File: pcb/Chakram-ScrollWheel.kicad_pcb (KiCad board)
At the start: 2 copper layers, 39.7 x 22.2 mm, 16 parts, among them J1 FPC Connector, SW1 RotaryEncoder

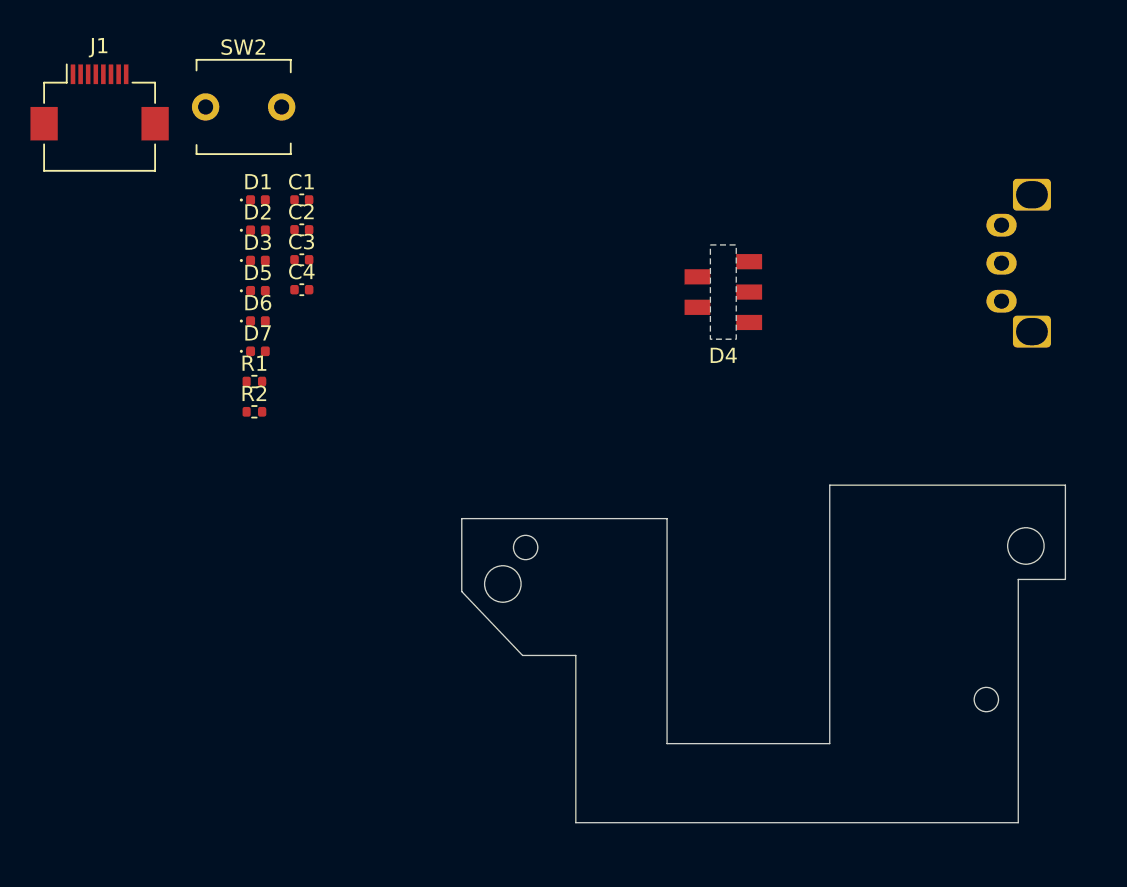
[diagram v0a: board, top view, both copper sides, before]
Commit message: Updated hole and component positions
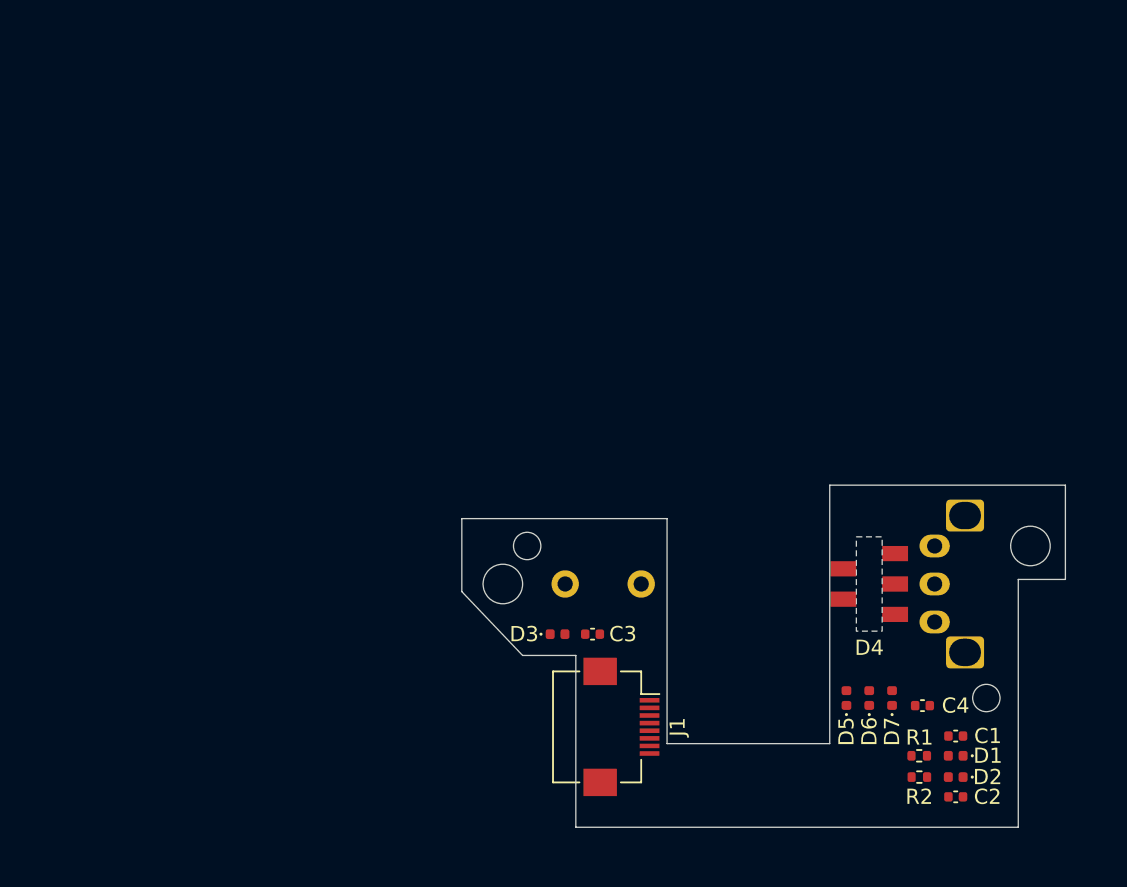
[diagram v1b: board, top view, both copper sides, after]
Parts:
- SW2: moved to B.Cu
- moved D1 58.7 mm to (87.5, 70.6), turned to 180 degrees
- moved D2 58.3 mm to (87.5, 72.0), turned to 180 degrees
- moved C2 56.9 mm to (87.5, 73.3)
- moved C1 55.6 mm to (87.5, 69.3)
- moved J1 53.5 mm to (65.5, 68.7), turned to -90 degrees
- moved R1 50.2 mm to (85.1, 70.6), turned to 180 degrees
- moved R2 49.9 mm to (85.1, 72.0), turned to 180 degrees
- moved C4 49.1 mm to (85.3, 67.3), turned to 180 degrees
- moved D7 47.5 mm to (83.3, 66.8), turned to 90 degrees
- moved D6 47.2 mm to (81.8, 66.8), turned to 90 degrees
- moved D5 47.1 mm to (80.3, 66.8), turned to 90 degrees
- moved SW2 39.3 mm to (64.3, 59.3), turned to 180 degrees
- moved D3 31.5 mm to (61.3, 62.6)
- moved C3 31.2 mm to (63.6, 62.6)
- moved SW1 21.6 mm to (86.1, 61.8)
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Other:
- board size 39.7 x 22.2 mm -> 39.7 x 22.5 mm

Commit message: Improved encoder symbol to also include  MP pins and connected them to GND
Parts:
- EN1: renamed from SW1; value RotaryEncoder -> RotaryEncoder_MP
- renumbered SW2 to SW1
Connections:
- EN1 pad MP: (no net) -> GND
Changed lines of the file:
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@@
 		(at 64.3 59.3 180)
 		(descr "Light Tactile Switch, https://api.pim.na.industrial.panasonic.com/file_stream/main/fileversion/245520")
-		(property "Reference" "SW2"
+		(property "Reference" "SW1"
 			(at 0 3.9 0)
 			(layer "B.SilkS")
@@
 		(descr "Alps rotary encoder, EC12E... with switch, vertical shaft, http://www.alps.com/prod/info/E/HTML/Encoder/Incremental/EC11/EC11E15204A3.html")
 		(tags "rotary encoder")
-		(property "Reference" "SW1"
+		(property "Reference" "EN1"
 			(at 4 -2.5 90)
 			(layer "B.SilkS")
@@
 			)
 		)
-		(property "Value" "RotaryEncoder"
+		(property "Value" "RotaryEncoder_MP"
 			(at 2 -9.5 0)
 			(layer "B.Fab")
@@
 			)
 		)
-		(property "Description" "Rotary encoder, dual channel, incremental quadrate outputs"
+		(property "Description" "Rotary encoder, dual channel, incremental quadrate outputs, with MP Pin"
 			(at 0 0 180)
 			(unlocked yes)
@@
 			(remove_unused_layers no)
 			(roundrect_rratio 0.125)
+			(net 1 "GND")
+			(pinfunction "MP")
+			(pintype "passive")
 		)
 		(pad "MP" thru_hole roundrect
@@
 			(remove_unused_layers no)
 			(roundrect_rratio 0.125)
+			(net 1 "GND")
+			(pinfunction "MP")
+			(pintype "passive")
 		)
 		(model "${MOUCHA_LIB}/Moucha.3dshapes/EC10E1220501.STEP"

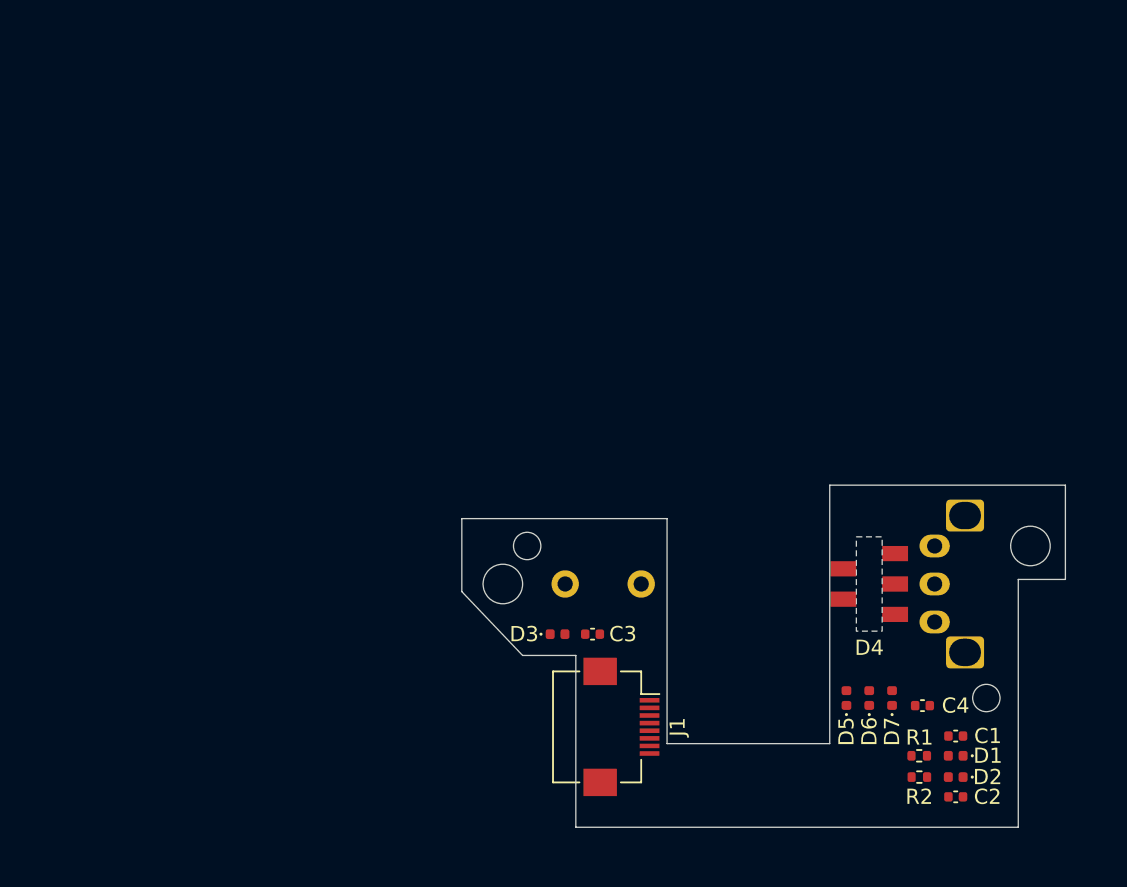
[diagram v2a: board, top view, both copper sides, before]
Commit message: Added testpoints
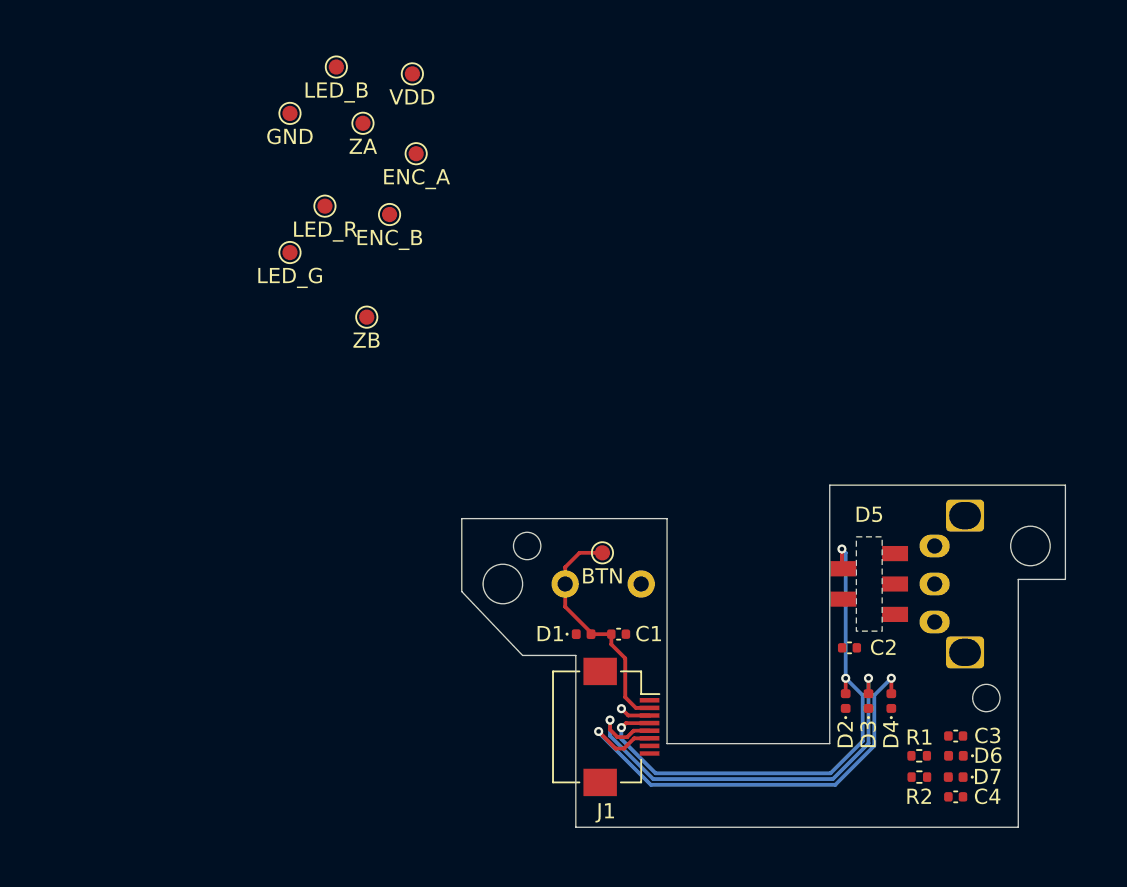
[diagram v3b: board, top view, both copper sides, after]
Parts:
- added TP1: VDD, TestPoint:TestPoint_Pad_D1.0mm, F.Cu at (51.8, 25.8)
- added TP10: ZB, TestPoint:TestPoint_Pad_D1.0mm, F.Cu at (48.8, 41.8)
- added TP2: GND, TestPoint:TestPoint_Pad_D1.0mm, F.Cu at (43.7, 28.4)
- added TP3: BTN, TestPoint:TestPoint_Pad_D1.0mm, F.Cu at (64.2, 57.2)
- added TP4: LED_R, TestPoint:TestPoint_Pad_D1.0mm, F.Cu at (46.0, 34.5)
- added TP5: LED_G, TestPoint:TestPoint_Pad_D1.0mm, F.Cu at (43.7, 37.5)
- added TP6: LED_B, TestPoint:TestPoint_Pad_D1.0mm, F.Cu at (46.8, 25.3)
- added TP7: ZA, TestPoint:TestPoint_Pad_D1.0mm, F.Cu at (48.5, 29.0)
- added TP8: ENC_A, TestPoint:TestPoint_Pad_D1.0mm, F.Cu at (52.0, 31.0)
- added TP9: ENC_B, TestPoint:TestPoint_Pad_D1.0mm, F.Cu at (50.2, 35.0)
- moved C2 6.12 mm to (80.5, 63.5), turned to 0 degrees
- moved D1 1.72 mm to (63.0, 62.6)
- moved C1 1.71 mm to (65.3, 62.6)
- moved D2 0.21 mm to (80.2, 67.0)
- moved D3 0.21 mm to (81.8, 67.0)
- moved D4 0.21 mm to (83.2, 67.0)
- renumbered C3 to C1, C4 to C2, C1 to C3, C2 to C4, D3 to D1, D5 to D2, D6 to D3, D7 to D4, D4 to D5, D1 to D6, D2 to D7
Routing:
- net /LED_R: track 0.00 -> 36.0 mm, vias 0 -> 3
- net /LED_B: track 0.00 -> 30.7 mm, vias 0 -> 2
- net /LED_G: track 0.00 -> 29.1 mm, vias 0 -> 2
- net /BTN: track 0.00 -> 15.7 mm
- net VDD: track 0.00 -> 2.04 mm, vias 0 -> 1

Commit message: Positioned all test points
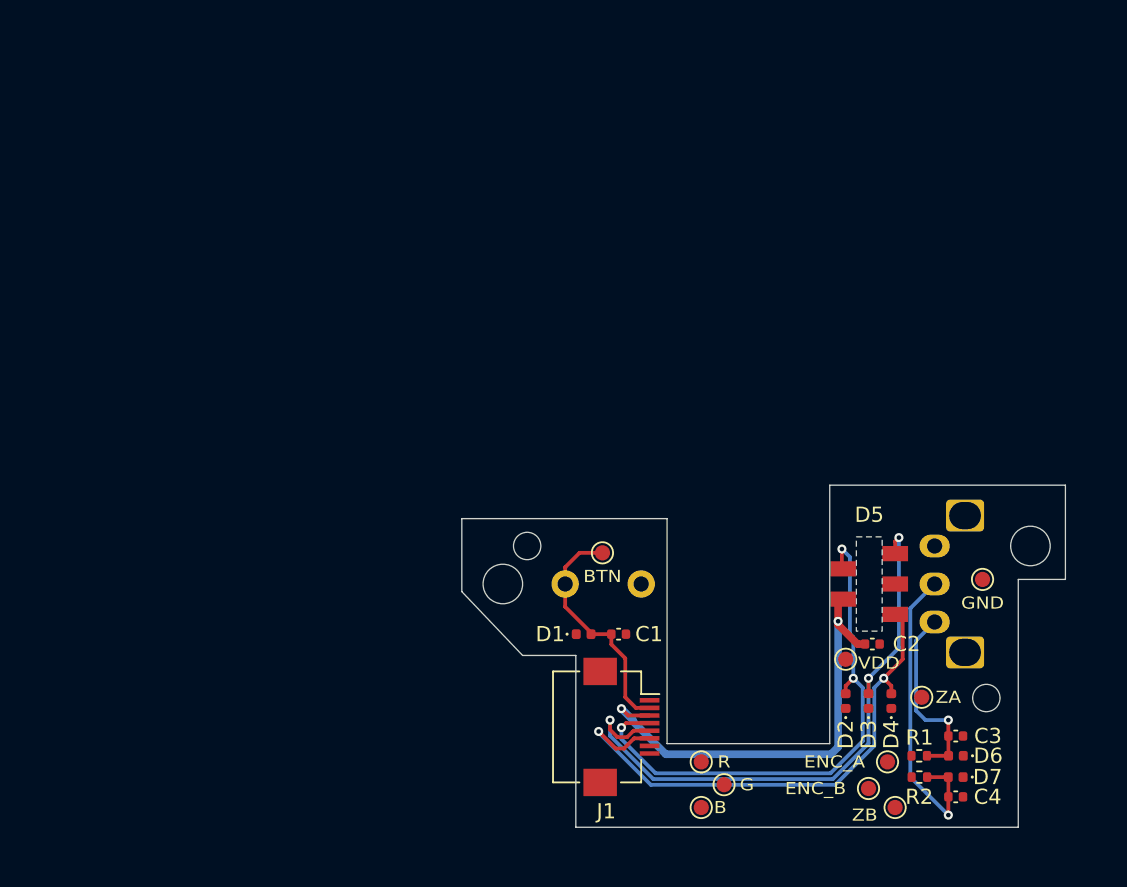
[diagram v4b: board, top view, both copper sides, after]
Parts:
- TP4: value LED_R -> R
- TP5: value LED_G -> G
- TP6: value LED_B -> B
- moved TP2 54.9 mm to (89.2, 59.0)
- moved TP6 54.3 mm to (70.8, 74.0)
- moved TP7 52.7 mm to (85.2, 66.8)
- moved TP8 50.6 mm to (83.0, 71.0)
- moved TP9 49.2 mm to (81.8, 72.8)
- moved TP1 47.9 mm to (80.2, 64.2)
- moved TP10 47.4 mm to (83.5, 74.0)
- moved TP5 45.2 mm to (72.2, 72.5)
- moved TP4 44.1 mm to (70.8, 71.0)
- moved C2 1.52 mm to (82.0, 63.2)
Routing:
- net VDD: track 2.04 -> 30.2 mm, vias 1 -> 2
- net /ZB: track 0.00 -> 20.8 mm, vias 0 -> 1
- net /ZA: track 0.00 -> 12.5 mm, vias 0 -> 1
- net /LED_G: track 29.1 -> 40.3 mm, vias 2 -> 3
- net /LED_B: track 30.7 -> 35.9 mm

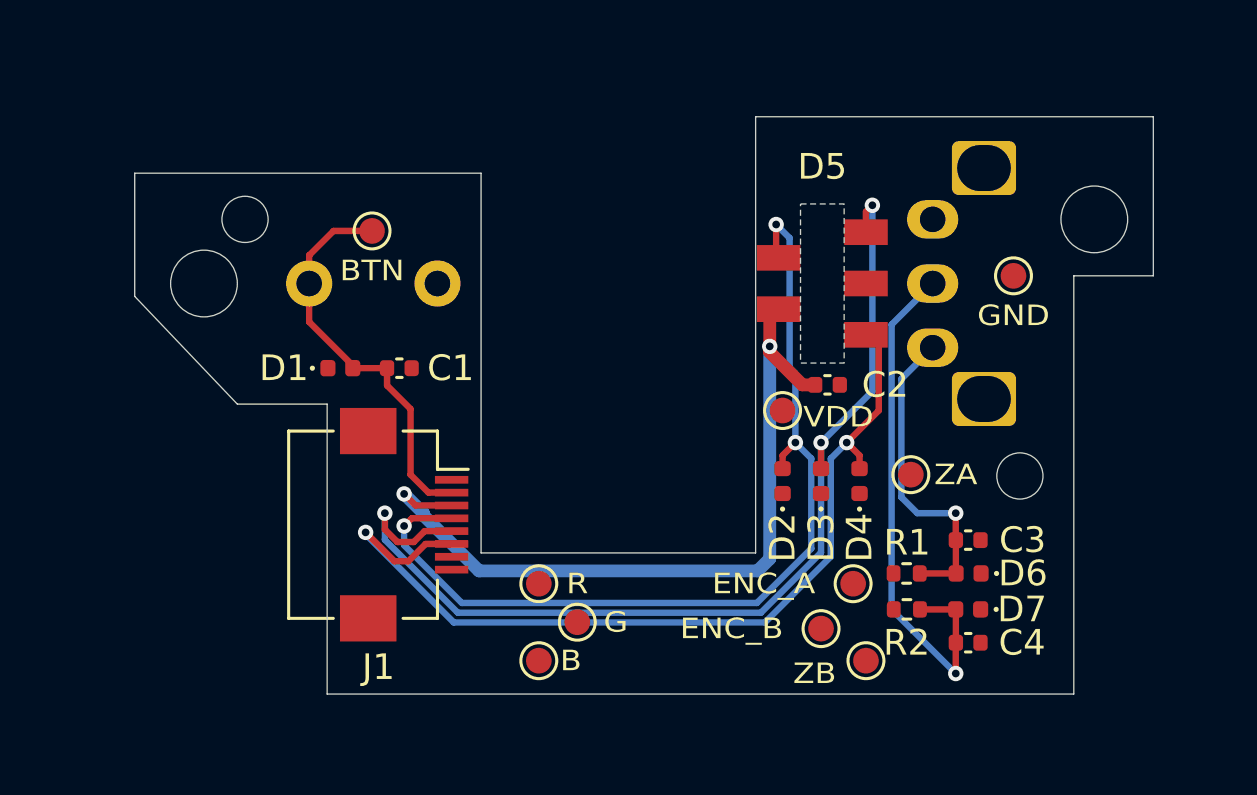
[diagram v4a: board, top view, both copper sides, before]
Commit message: Routed all signals
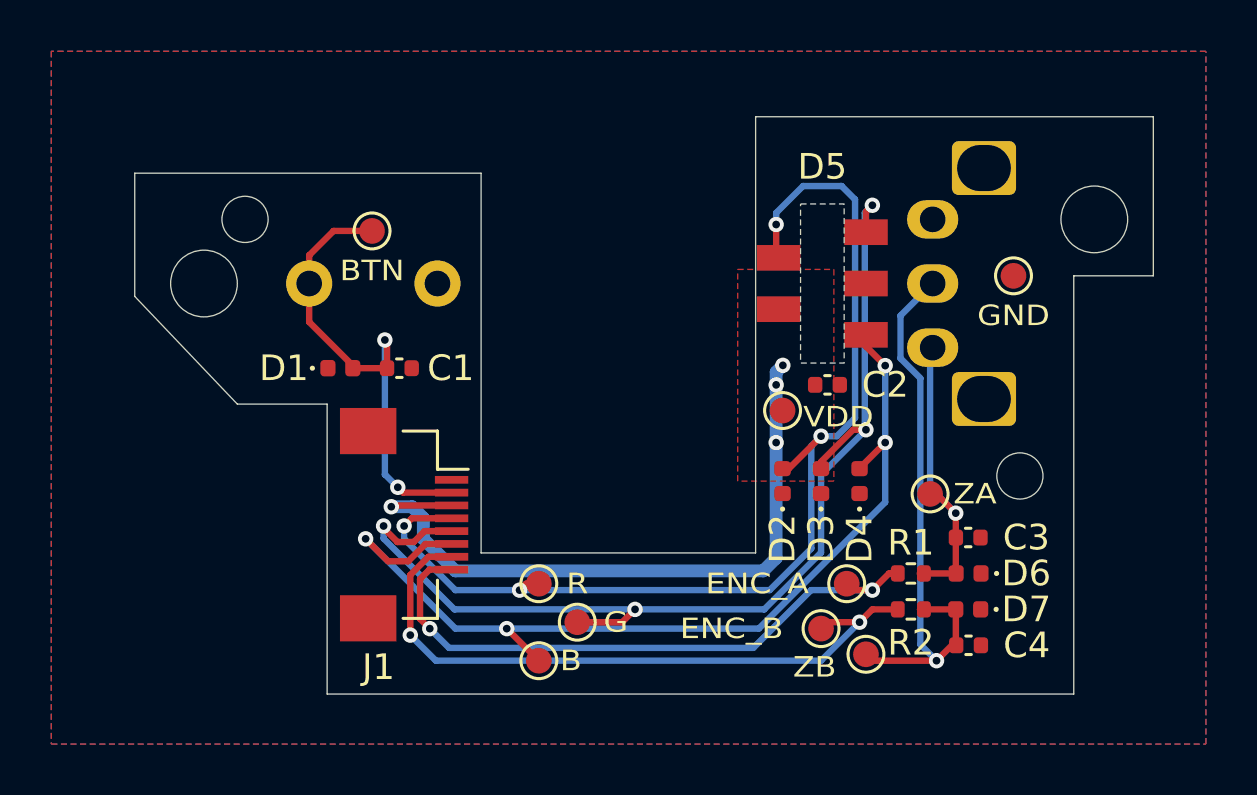
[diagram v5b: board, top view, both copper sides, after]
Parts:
- moved TP7 1.06 mm to (86.0, 67.5)
- moved TP10 0.25 mm to (83.5, 73.8)
- moved TP8 0.25 mm to (82.8, 71.0)
- moved R1 0.17 mm to (85.2, 70.6)
- moved R2 0.16 mm to (85.2, 72.0)
- moved C4 0.10 mm to (87.5, 73.4)
- moved C3 0.10 mm to (87.5, 69.2)
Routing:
- net /ENC_B: track 0.00 -> 25.9 mm, vias 0 -> 2
- net /ENC_A: track 0.00 -> 24.2 mm, vias 0 -> 2
- net /LED_R: track 36.2 -> 42.9 mm, vias 3 -> 4
- net VDD: track 30.2 -> 26.7 mm, vias 2 -> 4
- net /LED_G: track 40.3 -> 43.3 mm, vias 3 -> 4
- net /BTN: track 15.7 -> 18.6 mm, vias 0 -> 2
- net /LED_B: track 35.9 -> 37.8 mm, vias 2 -> 4
- net /ZB: track 20.8 -> 22.3 mm
- added copper zone on B.Cu, net GND
- added copper zone on F.Cu, net GND
- added copper zone on F.Cu, net VDD
